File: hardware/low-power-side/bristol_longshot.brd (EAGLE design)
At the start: 38 x 44.1 mm, 72 parts, among them U1 SAM_D20E, U10 ADP1607ACPZN-R7, U11 TPS73118DBVT, U2 SI4060, U3 SE880, U4 SST25WF040BT-40I/NP, U5 TG-5006CJ, U6 TG-5006CJ, U7 TPS3123, U8 SN74LVC1G32DCKR, U9 MS5607-02BA03, Y1 ABS05

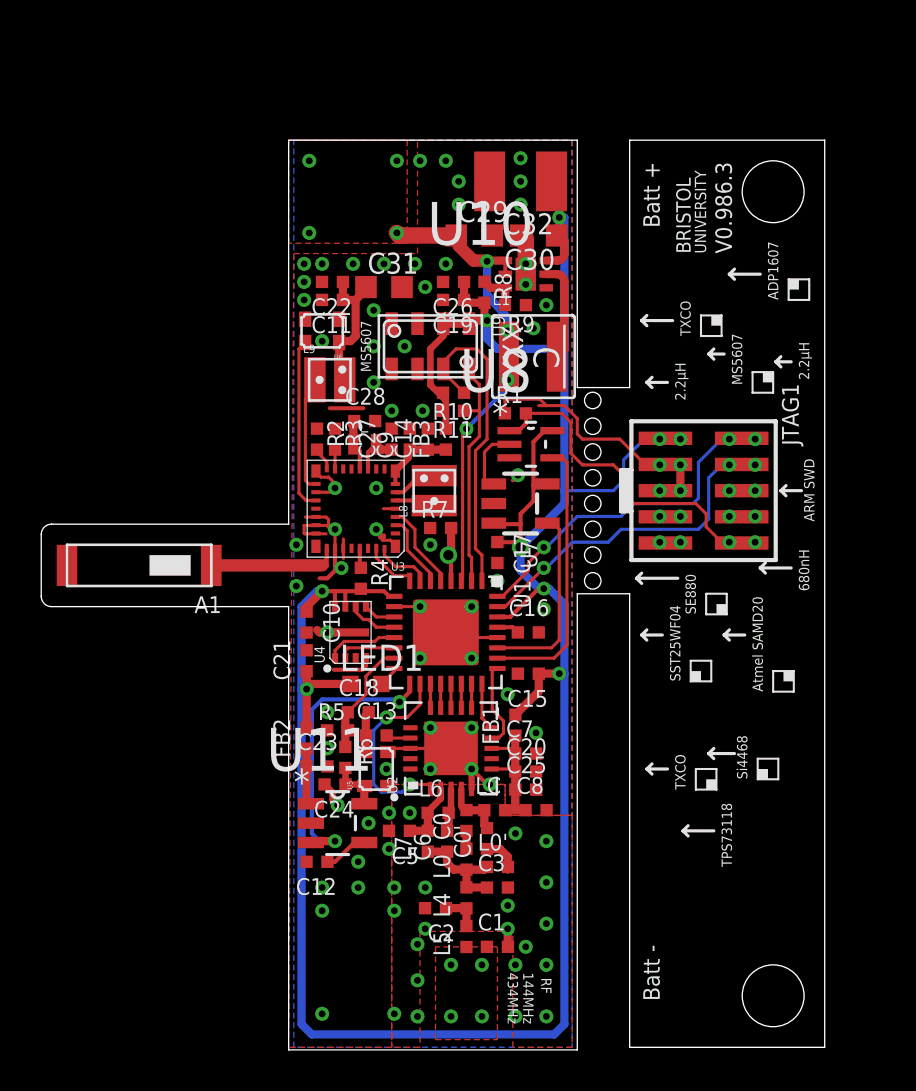
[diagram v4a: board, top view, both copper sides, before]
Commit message: low-power-side v0.986.4. Added LIS2D accelerometer. Optional
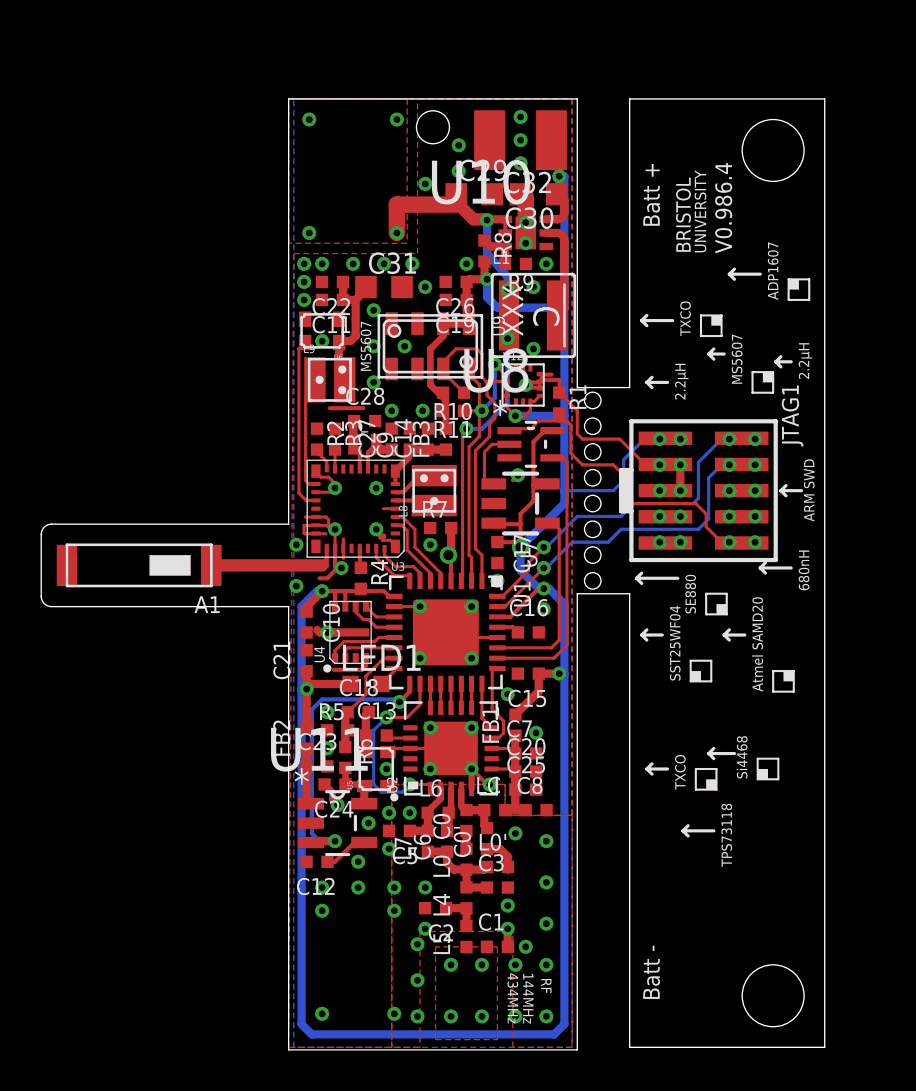
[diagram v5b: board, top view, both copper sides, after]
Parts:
- added U12: LIS2DH, fbri:LIS2DH
- moved R1 2.18 mm to (25.1, 31.2), turned to 270 degrees
- moved C29 2.00 mm to (21.0, 41.4)
- moved C30 2.00 mm to (24.1, 41.4)
- moved C32 2.00 mm to (23.2, 44.0)
- moved L1 2.00 mm to (23.9, 35.5)
- moved R8 2.00 mm to (21.5, 38.6)
- moved R9 2.00 mm to (23.0, 38.0)
- moved U10 2.00 mm to (23.5, 39.5)
- moved C19 0.12 mm to (20.1, 36.2)
- moved C26 0.12 mm to (20.1, 37.1)
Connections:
- net 1.8V: now also U12.3, U12.4, U12.7, U12.8
- net GND: now also U12.10, U12.11, U12.9
- net SCL: now also U12.1
- net SDA: now also U12.2
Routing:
- net 1.8V: track 134.2 -> 142.1 mm, vias 9 -> 10
- net 1.2V: track 23.7 -> 27.6 mm
- net SCL: track 11.5 -> 15.0 mm, vias 0 -> 2
- net SDA: track 15.6 -> 16.9 mm
- net GND: track 49.3 -> 49.7 mm, vias 86 -> 87
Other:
- board size 38 x 44.1 mm -> 38 x 46.1 mm
- board text added: "V0.986.4"
- board text removed: "V0.986.3"

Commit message: [low-power-side] v0.986.5 Added TS3006 low power clock
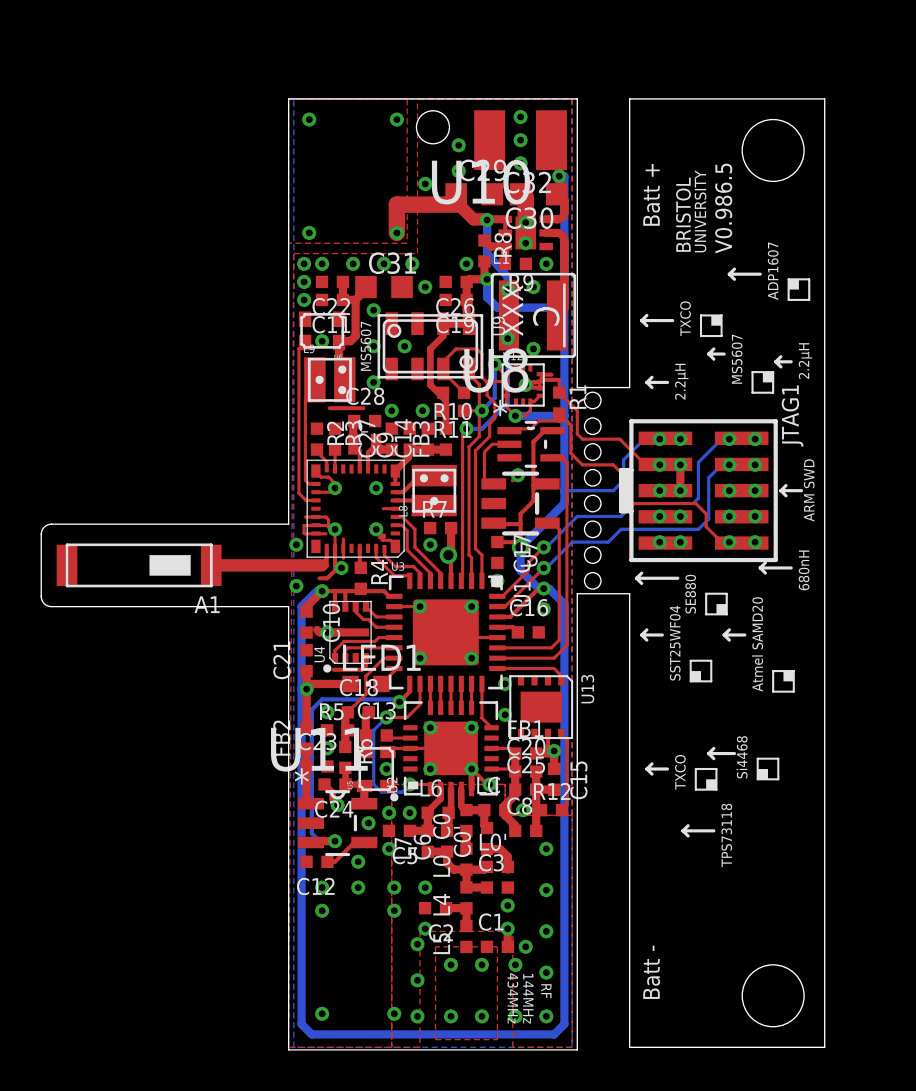
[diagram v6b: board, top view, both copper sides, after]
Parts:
- removed C7: 15pF, microbuilder_v3:_0402@2
- added R12: 4.32MΩ, microbuilder_v3:_0402
- added U13: TS3006, TS3006:TDFN33-8
- moved C15 5.28 mm to (24.9, 13.0), turned to 270 degrees
- moved FB1 1.46 mm to (23.5, 14.2), turned to 0 degrees
- moved C8 1.12 mm to (23.5, 10.5)
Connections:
- new net LF_CLOCK: U1.25, U13.1
- new net LF_RSET: R12.2, U13.8
- net 1.8V: now also U13.7
- net GND: now also R12.1, U13.3, U13.4, U13.5, U13.6, U13.PAD; no longer C7.2
- net RADIO_VDD: no longer C7.1
- net SI_GPIO0: no longer U1.25
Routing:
- net SI_GPIO0: track 4.36 -> 0.00 mm
- net GND: track 49.7 -> 53.9 mm
- net LF_RSET: track 0.00 -> 3.93 mm
- net LF_CLOCK: track 0.00 -> 3.48 mm
- net RADIO_VDD: track 8.18 -> 6.70 mm
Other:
- board text added: "V0.986.5"
- board text removed: "V0.986.4"

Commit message: [low power] v0.986.6. Added LDO for GPS, LF TCXO for GPS
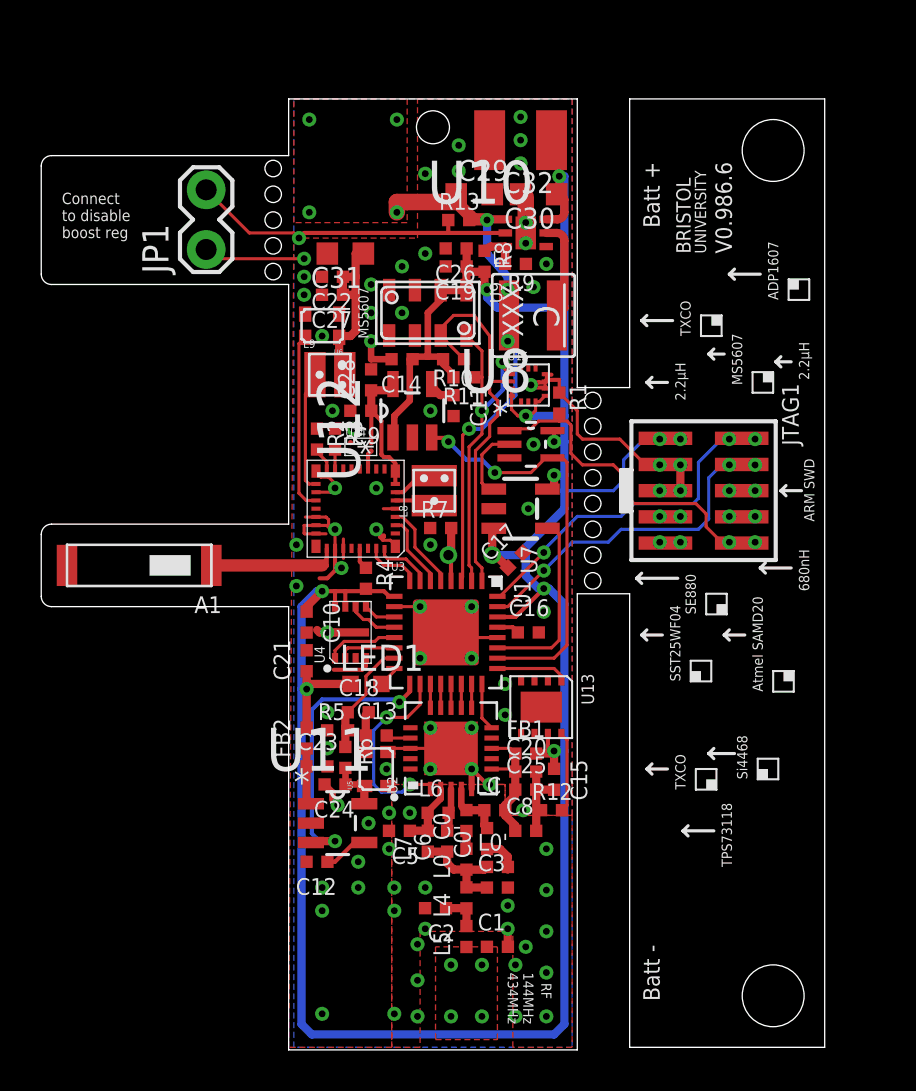
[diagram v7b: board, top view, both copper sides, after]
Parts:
- removed FB3: (no value), microbuilder_v3:_0402@1
- removed Y1: ABS05, fbri:ABS05
- added JP1: (no value), SparkFun:1X02_LOCK
- added R13: 10kΩ, microbuilder_v3:_0402
- added U14: SIT1552, fbri:SIT1552
- added U15: LIS2DH, fbri:LIS2DH
- C11: value 1nF -> 10nF
- C27: value 18pF -> 1nF
- C28: value 18pF -> 1µF
- U12: value LIS2DH -> TPS73118DBVT; device fbri:LIS2DH -> TPS73118DVBT:SOT95P280X145-5N
- moved C11 7.80 mm to (20.0, 31.1), turned to 270 degrees
- moved C27 7.57 mm to (14.1, 36.5), turned to 180 degrees
- moved U12 5.52 mm to (18.0, 30.9), turned to 90 degrees
- moved C14 4.07 mm to (17.5, 33.4), turned to 180 degrees
- moved C9 2.74 mm to (15.5, 30.9), turned to 180 degrees
- moved C31 2.48 mm to (14.8, 38.5), turned to 180 degrees
- moved C28 2.02 mm to (16.0, 32.4), turned to 90 degrees
- moved R11 1.70 mm to (20.5, 32.5)
- moved U9 1.63 mm to (18.8, 35.6)
- moved C19 1.62 mm to (20.1, 37.9)
- moved C26 1.62 mm to (20.1, 38.8)
- moved R10 1.62 mm to (20.0, 33.4)
- moved C17 0.95 mm to (23.0, 23.6), turned to 45 degrees
- moved R8 0.50 mm to (21.5, 38.1)
- moved C22 0.25 mm to (14.1, 37.4)
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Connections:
- new net BOOST_EN: JP1.2, R13.1, U10.2
- new net GPS_REG_NR: C11.1, U12.4
- net !RESET: now also U12.3
- net 1.2V: now also R13.2; no longer U10.2
- net 1.8V: now also C14.1, U12.1, U15.3, U15.4, U15.7, U15.8; no longer FB3.2, U12.3, U12.4, U12.7, U12.8
- net GND: now also JP1.1, U12.2, U14.1, U14.4, U15.10, U15.11, U15.9; no longer U12.10, U12.11, U12.9
- net GPS_VDD: now also C28.1, U12.5, U14.3; no longer C14.1, FB3.1
- net RTC_XI: now also U14.2; no longer C27.1, Y1.1
- net RTC_XO: no longer C28.1, Y1.2
- net SCL: now also U15.1; no longer U12.1
- net SDA: now also U15.2; no longer U12.2
- net TCXO_VDD1: now also C27.1; no longer C11.1
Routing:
- net BOOST_EN: track 0.00 -> 16.2 mm, vias 0 -> 1
- net !RESET: track 13.3 -> 20.2 mm, vias 0 -> 2
- net GND: track 53.9 -> 58.5 mm, vias 87 -> 83
- net GPS_VDD: track 3.69 -> 8.10 mm
- net RTC_XO: track 2.46 -> 0.00 mm
- net TCXO_VDD1: track 6.93 -> 9.10 mm
- net SDA: track 16.9 -> 18.8 mm
- net SCL: track 15.0 -> 16.8 mm
- net GPS_REG_NR: track 0.00 -> 1.36 mm
- net RTC_XI: track 2.23 -> 0.93 mm
- net 1.2V: track 27.6 -> 26.4 mm
- net 1.8V: track 141.9 -> 141.5 mm, vias 10 -> 12
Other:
- outline, holes or cut-outs redrawn
- board text added: "Connect to disable boost reg"
- board text added: "V0.986.6"
- board text removed: "V0.986.5"

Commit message: [low power] v0.986.7. Changed low power lf clock, added vreg on breakout for optional power testing
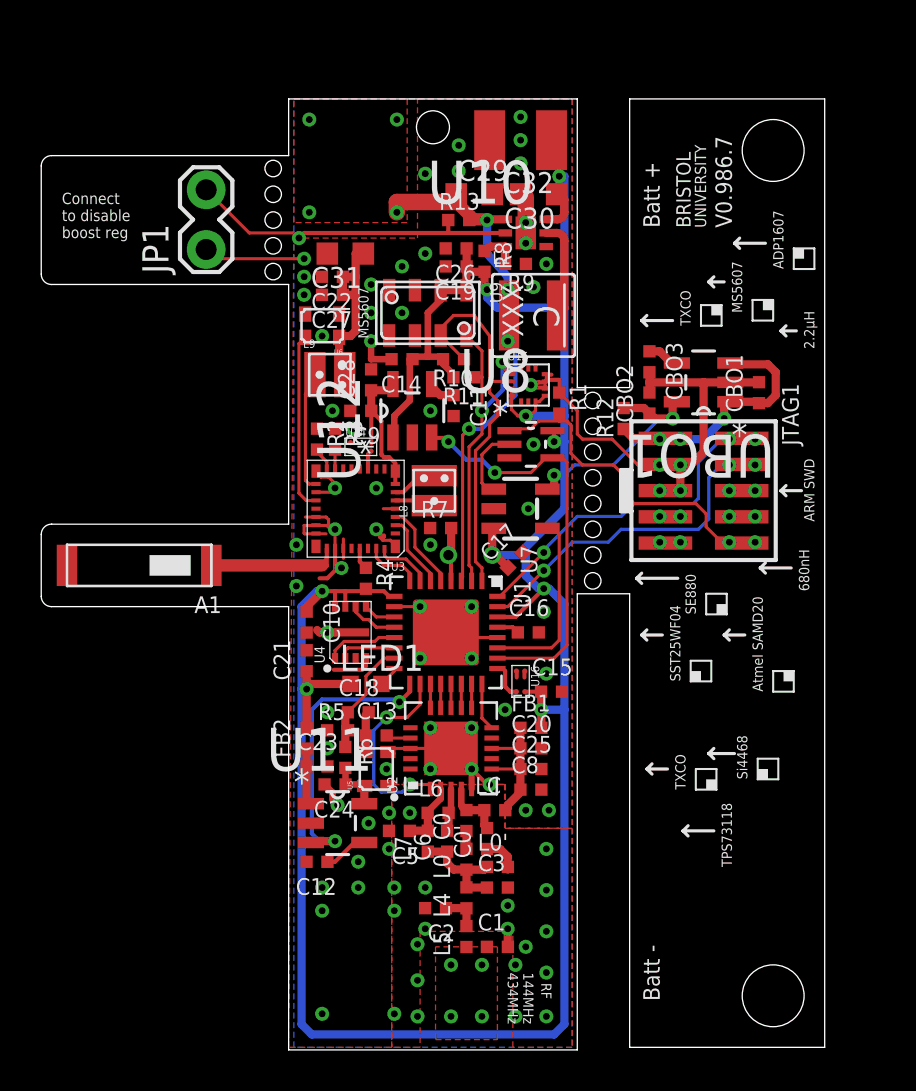
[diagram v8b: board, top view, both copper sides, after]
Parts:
- removed U13: TS3006, TS3006:TDFN33-8
- added CBO1, CBO2: 1µF, microbuilder_v3:_0402@2
- added CBO3: 10nF, microbuilder_v3:_0402@2
- added U16: SIT1552, fbri:SIT1552
- added UBO1: TPS73118DBVT, TPS73118DVBT:SOT95P280X145-5N
- R12: value 4.32MΩ -> 0Ω
- moved R12 19.3 mm to (28.2, 30.5), turned to 90 degrees
- moved C15 4.25 mm to (24.8, 17.2), turned to 0 degrees
- moved C8 2.02 mm to (23.8, 12.5)
- moved FB1 1.27 mm to (23.8, 15.5)
- moved C20 1.15 mm to (23.8, 14.5)
- moved C25 1.03 mm to (23.8, 13.5)
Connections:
- removed net LF_RSET: R12.2, U13.8
- new net JTAG_VIN: CBO1.1, JTAG1.1, R12.1, UBO1.1, UBO1.3
- new net JTAG_VREG_NR: CBO3.1, UBO1.4
- net 1.8V: now also CBO2.1, R12.2, U16.3, UBO1.5; no longer JTAG1.1, U13.7
- net GND: now also CBO1.2, CBO2.2, CBO3.2, U16.1, U16.4, UBO1.2; no longer R12.1, U13.3, U13.4, U13.5, U13.6, U13.PAD
- net LF_CLOCK: now also U16.2; no longer U13.1
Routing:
- net JTAG_VIN: track 0.00 -> 12.6 mm, vias 0 -> 3
- net GND: track 58.5 -> 66.4 mm, vias 83 -> 84
- net LF_RSET: track 3.93 -> 0.00 mm
- net 1.8V: track 141.5 -> 144.4 mm, vias 12 -> 11
- net LF_CLOCK: track 3.48 -> 1.83 mm
- net JTAG_VREG_NR: track 0.00 -> 1.56 mm
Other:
- board text added: "V0.986.7"
- board text removed: "V0.986.6"
